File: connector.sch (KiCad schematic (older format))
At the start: 3 parts, among them J1 DB26_Male_HighDensity_Mountin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, J6 Conn_02x02_Odd_Even

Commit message: create footprints
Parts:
- J6: footprint (none) -> Connector_PinHeader_2.54mm:PinHeader_2x02_P2.54mm_Vertical
- SW3: renamed from SW?; footprint (none) -> Button_Switch_THT:SW_DIP_SPSTx03_Slide_9.78x9.8mm_W7.62mm_P2.54mm
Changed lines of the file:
@@
 $Descr A4 11693 8268
 encoding utf-8
-Sheet 7 17
+Sheet 17 17
 Title ""
 Date ""
@@
 AR Path="/5F112860/5F10EEE2/5F14DCB5" Ref="J14"  Part="1"
 AR Path="/5F112863/5F10EEE2/5F14DCB5" Ref="J16"  Part="1"
-F 0 "J6" H 5425 6217 50  0000 C CNN
+F 0 "J16" H 5425 6217 50  0000 C CNN
 F 1 "DB26_Male_HighDensity_MountingHoles" H 5425 6126 50  0000 C CNN
 F 2 "Connector_Dsub:DSUB-26-HD_Male_Horizontal_P2.29x1.98mm_EdgePinOffset3.03mm_Housed_MountingHolesOffset4.94mm" H 4475 5000 50  0001 C CNN
@@
 AR Path="/5F112860/5F10EEE2/5F139BC3" Ref="J15"  Part="1"
 AR Path="/5F112863/5F10EEE2/5F139BC3" Ref="J17"  Part="1"
-F 0 "J7" H 5550 2100 50  0000 C CNN
+F 0 "J17" H 5550 2100 50  0000 C CNN
 F 1 "Conn_02x02_Odd_Even" H 5550 2191 50  0000 C CNN
-F 2 "" H 5500 2425 50  0001 C CNN
+F 2 "Connector_PinHeader_2.54mm:PinHeader_2x02_P2.54mm_Vertical" H 5500 2425 50  0001 C CNN
 F 3 "~" H 5500 2425 50  0001 C CNN
 	1    5500 2425
@@
 AR Path="/5F112860/5F10EEE2/5F4B7169" Ref="#PWR031"  Part="1"
 AR Path="/5F112863/5F10EEE2/5F4B7169" Ref="#PWR034"  Part="1"
-F 0 "#PWR019" H 4525 3150 50  0001 C CNN
+F 0 "#PWR034" H 4525 3150 50  0001 C CNN
 F 1 "GND" H 4530 3227 50  0000 C CNN
 F 2 "" H 4525 3400 50  0001 C CNN
@@
 AR Path="/5F112860/5F10EEE2/5F4B88F0" Ref="#PWR032"  Part="1"
 AR Path="/5F112863/5F10EEE2/5F4B88F0" Ref="#PWR035"  Part="1"
-F 0 "#PWR020" H 5425 5050 50  0001 C CNN
+F 0 "#PWR035" H 5425 5050 50  0001 C CNN
 F 1 "GND" H 5430 5127 50  0000 C CNN
 F 2 "" H 5425 5300 50  0001 C CNN
@@
 5V
 $Comp
-L Switch:SW_DIP_x03 SW?
+L Switch:SW_DIP_x03 SW3
 U 1 1 5F14E492
 P 2975 3575
-AR Path="/5F1123F9/5F10EEE2/5F14E492" Ref="SW?"  Part="1"
-AR Path="/5F11264C/5F10EEE2/5F14E492" Ref="SW?"  Part="1"
-F 0 "SW?" H 2975 4042 50  0000 C CNN
+AR Path="/5F1123F9/5F10EEE2/5F14E492" Ref="SW3"  Part="1"
+AR Path="/5F11264C/5F10EEE2/5F14E492" Ref="SW4"  Part="1"
+AR Path="/5F10DACE/5F10EEE2/5F14E492" Ref="SW2"  Part="1"
+AR Path="/5F11264F/5F10EEE2/5F14E492" Ref="SW5"  Part="1"
+AR Path="/5F11285A/5F10EEE2/5F14E492" Ref="SW6"  Part="1"
+AR Path="/5F11285D/5F10EEE2/5F14E492" Ref="SW7"  Part="1"
+AR Path="/5F112860/5F10EEE2/5F14E492" Ref="SW8"  Part="1"
+AR Path="/5F112863/5F10EEE2/5F14E492" Ref="SW9"  Part="1"
+F 0 "SW9" H 2975 4042 50  0000 C CNN
 F 1 "SW_DIP_x03" H 2975 3951 50  0000 C CNN
-F 2 "" H 2975 3575 50  0001 C CNN
+F 2 "Button_Switch_THT:SW_DIP_SPSTx03_Slide_9.78x9.8mm_W7.62mm_P2.54mm" H 2975 3575 50  0001 C CNN
 F 3 "~" H 2975 3575 50  0001 C CNN
 	1    2975 3575
@@
 AR Path="/5F112860/5F10EEE2/5F4B6D92" Ref="#PWR030"  Part="1"
 AR Path="/5F112863/5F10EEE2/5F4B6D92" Ref="#PWR033"  Part="1"
-F 0 "#PWR018" H 2675 3225 50  0001 C CNN
+F 0 "#PWR033" H 2675 3225 50  0001 C CNN
 F 1 "VCC" V 2675 3575 50  0000 C CNN
 F 2 "" H 2675 3375 50  0001 C CNN

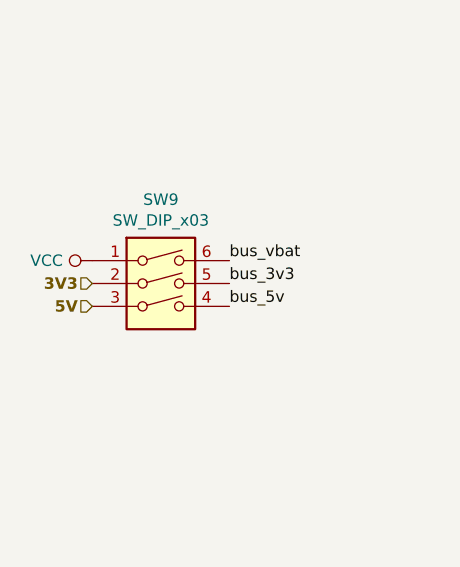
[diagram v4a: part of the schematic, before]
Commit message: rework power management schematic
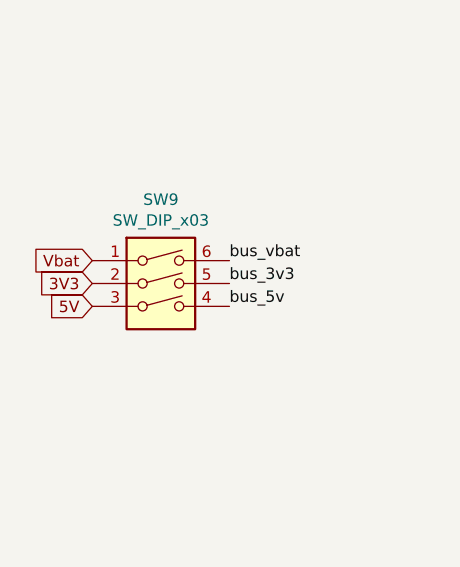
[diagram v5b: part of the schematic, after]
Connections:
- net VCC renamed Vbat
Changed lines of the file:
@@
 $Descr A4 11693 8268
 encoding utf-8
-Sheet 17 17
+Sheet 2 9
 Title ""
 Date ""
@@
 AR Path="/5F112860/5F10EEE2/5F14DCB5" Ref="J14"  Part="1"
 AR Path="/5F112863/5F10EEE2/5F14DCB5" Ref="J16"  Part="1"
+AR Path="/5F1F8EB1/5F14DCB5" Ref="J2"  Part="1"
+AR Path="/5F202513/5F14DCB5" Ref="J?"  Part="1"
+AR Path="/5F214496/5F14DCB5" Ref="J?"  Part="1"
+AR Path="/5F2144C2/5F14DCB5" Ref="J?"  Part="1"
+AR Path="/5F21C578/5F14DCB5" Ref="J?"  Part="1"
+AR Path="/5F21C5A4/5F14DCB5" Ref="J?"  Part="1"
+AR Path="/5F21C5D0/5F14DCB5" Ref="J?"  Part="1"
+AR Path="/5F21C5FC/5F14DCB5" Ref="J?"  Part="1"
+AR Path="/5F22A1CE/5F14DCB5" Ref="J4"  Part="1"
+AR Path="/5F22D207/5F14DCB5" Ref="J6"  Part="1"
+AR Path="/5F22D233/5F14DCB5" Ref="J8"  Part="1"
+AR Path="/5F2317AE/5F14DCB5" Ref="J10"  Part="1"
+AR Path="/5F2317DA/5F14DCB5" Ref="J12"  Part="1"
+AR Path="/5F237BED/5F14DCB5" Ref="J14"  Part="1"
+AR Path="/5F237C19/5F14DCB5" Ref="J16"  Part="1"
 F 0 "J16" H 5425 6217 50  0000 C CNN
 F 1 "DB26_Male_HighDensity_MountingHoles" H 5425 6126 50  0000 C CNN
@@
 AR Path="/5F112860/5F10EEE2/5F139BC3" Ref="J15"  Part="1"
 AR Path="/5F112863/5F10EEE2/5F139BC3" Ref="J17"  Part="1"
+AR Path="/5F1F8EB1/5F139BC3" Ref="J3"  Part="1"
+AR Path="/5F202513/5F139BC3" Ref="J?"  Part="1"
+AR Path="/5F214496/5F139BC3" Ref="J?"  Part="1"
+AR Path="/5F2144C2/5F139BC3" Ref="J?"  Part="1"
+AR Path="/5F21C578/5F139BC3" Ref="J?"  Part="1"
+AR Path="/5F21C5A4/5F139BC3" Ref="J?"  Part="1"
+AR Path="/5F21C5D0/5F139BC3" Ref="J?"  Part="1"
+AR Path="/5F21C5FC/5F139BC3" Ref="J?"  Part="1"
+AR Path="/5F22A1CE/5F139BC3" Ref="J5"  Part="1"
+AR Path="/5F22D207/5F139BC3" Ref="J7"  Part="1"
+AR Path="/5F22D233/5F139BC3" Ref="J9"  Part="1"
+AR Path="/5F2317AE/5F139BC3" Ref="J11"  Part="1"
+AR Path="/5F2317DA/5F139BC3" Ref="J13"  Part="1"
+AR Path="/5F237BED/5F139BC3" Ref="J15"  Part="1"
+AR Path="/5F237C19/5F139BC3" Ref="J17"  Part="1"
 F 0 "J17" H 5550 2100 50  0000 C CNN
 F 1 "Conn_02x02_Odd_Even" H 5550 2191 50  0000 C CNN
@@
 AR Path="/5F112860/5F10EEE2/5F4B7169" Ref="#PWR031"  Part="1"
 AR Path="/5F112863/5F10EEE2/5F4B7169" Ref="#PWR034"  Part="1"
-F 0 "#PWR034" H 4525 3150 50  0001 C CNN
+AR Path="/5F1F8EB1/5F4B7169" Ref="#PWR0102"  Part="1"
+AR Path="/5F202513/5F4B7169" Ref="#PWR?"  Part="1"
+AR Path="/5F214496/5F4B7169" Ref="#PWR?"  Part="1"
+AR Path="/5F2144C2/5F4B7169" Ref="#PWR?"  Part="1"
+AR Path="/5F21C578/5F4B7169" Ref="#PWR?"  Part="1"
+AR Path="/5F21C5A4/5F4B7169" Ref="#PWR?"  Part="1"
+AR Path="/5F21C5D0/5F4B7169" Ref="#PWR?"  Part="1"
+AR Path="/5F21C5FC/5F4B7169" Ref="#PWR?"  Part="1"
+AR Path="/5F22A1CE/5F4B7169" Ref="#PWR0105"  Part="1"
+AR Path="/5F22D207/5F4B7169" Ref="#PWR0108"  Part="1"
+AR Path="/5F22D233/5F4B7169" Ref="#PWR0111"  Part="1"
+AR Path="/5F2317AE/5F4B7169" Ref="#PWR0114"  Part="1"
+AR Path="/5F2317DA/5F4B7169" Ref="#PWR0117"  Part="1"
+AR Path="/5F237BED/5F4B7169" Ref="#PWR0120"  Part="1"
+AR Path="/5F237C19/5F4B7169" Ref="#PWR0123"  Part="1"
+F 0 "#PWR0123" H 4525 3150 50  0001 C CNN
 F 1 "GND" H 4530 3227 50  0000 C CNN
 F 2 "" H 4525 3400 50  0001 C CNN
@@
 AR Path="/5F112860/5F10EEE2/5F4B88F0" Ref="#PWR032"  Part="1"
 AR Path="/5F112863/5F10EEE2/5F4B88F0" Ref="#PWR035"  Part="1"
-F 0 "#PWR035" H 5425 5050 50  0001 C CNN
+AR Path="/5F1F8EB1/5F4B88F0" Ref="#PWR0103"  Part="1"
+AR Path="/5F202513/5F4B88F0" Ref="#PWR?"  Part="1"
+AR Path="/5F214496/5F4B88F0" Ref="#PWR?"  Part="1"
+AR Path="/5F2144C2/5F4B88F0" Ref="#PWR?"  Part="1"
+AR Path="/5F21C578/5F4B88F0" Ref="#PWR?"  Part="1"
+AR Path="/5F21C5A4/5F4B88F0" Ref="#PWR?"  Part="1"
+AR Path="/5F21C5D0/5F4B88F0" Ref="#PWR?"  Part="1"
+AR Path="/5F21C5FC/5F4B88F0" Ref="#PWR?"  Part="1"
+AR Path="/5F22A1CE/5F4B88F0" Ref="#PWR0106"  Part="1"
+AR Path="/5F22D207/5F4B88F0" Ref="#PWR0109"  Part="1"
+AR Path="/5F22D233/5F4B88F0" Ref="#PWR0112"  Part="1"
+AR Path="/5F2317AE/5F4B88F0" Ref="#PWR0115"  Part="1"
+AR Path="/5F2317DA/5F4B88F0" Ref="#PWR0118"  Part="1"
+AR Path="/5F237BED/5F4B88F0" Ref="#PWR0121"  Part="1"
+AR Path="/5F237C19/5F4B88F0" Ref="#PWR0124"  Part="1"
+F 0 "#PWR0124" H 5425 5050 50  0001 C CNN
 F 1 "GND" H 5430 5127 50  0000 C CNN
 F 2 "" H 5425 5300 50  0001 C CNN
@@
 	1    0    0    -1
 $EndComp
-Text HLabel 2675 3475 0    50   Input ~ 10
-3V3
-Text HLabel 2675 3575 0    50   Input ~ 10
-5V
 $Comp
 L Switch:SW_DIP_x03 SW3
@@
 AR Path="/5F112860/5F10EEE2/5F14E492" Ref="SW8"  Part="1"
 AR Path="/5F112863/5F10EEE2/5F14E492" Ref="SW9"  Part="1"
+AR Path="/5F1F8EB1/5F14E492" Ref="SW2"  Part="1"
+AR Path="/5F202513/5F14E492" Ref="SW?"  Part="1"
+AR Path="/5F214496/5F14E492" Ref="SW?"  Part="1"
+AR Path="/5F2144C2/5F14E492" Ref="SW?"  Part="1"
+AR Path="/5F21C578/5F14E492" Ref="SW?"  Part="1"
+AR Path="/5F21C5A4/5F14E492" Ref="SW?"  Part="1"
+AR Path="/5F21C5D0/5F14E492" Ref="SW?"  Part="1"
+AR Path="/5F21C5FC/5F14E492" Ref="SW?"  Part="1"
+AR Path="/5F22A1CE/5F14E492" Ref="SW3"  Part="1"
+AR Path="/5F22D207/5F14E492" Ref="SW4"  Part="1"
+AR Path="/5F22D233/5F14E492" Ref="SW5"  Part="1"
+AR Path="/5F2317AE/5F14E492" Ref="SW6"  Part="1"
+AR Path="/5F2317DA/5F14E492" Ref="SW7"  Part="1"
+AR Path="/5F237BED/5F14E492" Ref="SW8"  Part="1"
+AR Path="/5F237C19/5F14E492" Ref="SW9"  Part="1"
 F 0 "SW9" H 2975 4042 50  0000 C CNN
 F 1 "SW_DIP_x03" H 2975 3951 50  0000 C CNN
@@
 	1    2975 3575
 	1    0    0    -1
-$EndComp
-$Comp
-L power:VCC #PWR012
-U 1 1 5F4B6D92
-P 2675 3375
-AR Path="/5F10DACE/5F10EEE2/5F4B6D92" Ref="#PWR012"  Part="1"
-AR Path="/5F1100AF/5F10EEE2/5F4B6D92" Ref="#PWR?"  Part="1"
-AR Path="/5F1100FD/5F10EEE2/5F4B6D92" Ref="#PWR?"  Part="1"
-AR Path="/5F110145/5F10EEE2/5F4B6D92" Ref="#PWR?"  Part="1"
-AR Path="/5F11031E/5F10EEE2/5F4B6D92" Ref="#PWR?"  Part="1"
-AR Path="/5F110320/5F10EEE2/5F4B6D92" Ref="#PWR?"  Part="1"
-AR Path="/5F110322/5F10EEE2/5F4B6D92" Ref="#PWR?"  Part="1"
-AR Path="/5F110324/5F10EEE2/5F4B6D92" Ref="#PWR?"  Part="1"
-AR Path="/5F1123F9/5F10EEE2/5F4B6D92" Ref="#PWR015"  Part="1"
-AR Path="/5F11264C/5F10EEE2/5F4B6D92" Ref="#PWR018"  Part="1"
-AR Path="/5F11264F/5F10EEE2/5F4B6D92" Ref="#PWR021"  Part="1"
-AR Path="/5F11285A/5F10EEE2/5F4B6D92" Ref="#PWR024"  Part="1"
-AR Path="/5F11285D/5F10EEE2/5F4B6D92" Ref="#PWR027"  Part="1"
-AR Path="/5F112860/5F10EEE2/5F4B6D92" Ref="#PWR030"  Part="1"
-AR Path="/5F112863/5F10EEE2/5F4B6D92" Ref="#PWR033"  Part="1"
-F 0 "#PWR033" H 2675 3225 50  0001 C CNN
-F 1 "VCC" V 2675 3575 50  0000 C CNN
-F 2 "" H 2675 3375 50  0001 C CNN
-F 3 "" H 2675 3375 50  0001 C CNN
-	1    2675 3375
-	0    -1   -1   0
 $EndComp
 Text Label 3275 3375 0    50   ~ 0
@@
 Text Label 5725 3500 0    50   ~ 0
 bus_3v3
+Text GLabel 2675 3375 0    50   Input ~ 0
+Vbat
+Text GLabel 2675 3475 0    50   Input ~ 0
+3V3
+Text GLabel 2675 3575 0    50   Input ~ 0
+5V
 $EndSCHEMATC

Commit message: try improving positionning
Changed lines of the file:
@@
 AR Path="/5F237BED/5F14DCB5" Ref="J14"  Part="1"
 AR Path="/5F237C19/5F14DCB5" Ref="J16"  Part="1"
-F 0 "J16" H 5425 6217 50  0000 C CNN
+F 0 "J2" H 5425 6217 50  0000 C CNN
 F 1 "DB26_Male_HighDensity_MountingHoles" H 5425 6126 50  0000 C CNN
 F 2 "Connector_Dsub:DSUB-26-HD_Male_Horizontal_P2.29x1.98mm_EdgePinOffset3.03mm_Housed_MountingHolesOffset4.94mm" H 4475 5000 50  0001 C CNN
@@
 AR Path="/5F237BED/5F139BC3" Ref="J15"  Part="1"
 AR Path="/5F237C19/5F139BC3" Ref="J17"  Part="1"
-F 0 "J17" H 5550 2100 50  0000 C CNN
+F 0 "J3" H 5550 2100 50  0000 C CNN
 F 1 "Conn_02x02_Odd_Even" H 5550 2191 50  0000 C CNN
 F 2 "Connector_PinHeader_2.54mm:PinHeader_2x02_P2.54mm_Vertical" H 5500 2425 50  0001 C CNN
@@
 AR Path="/5F237BED/5F4B7169" Ref="#PWR0120"  Part="1"
 AR Path="/5F237C19/5F4B7169" Ref="#PWR0123"  Part="1"
-F 0 "#PWR0123" H 4525 3150 50  0001 C CNN
+F 0 "#PWR0102" H 4525 3150 50  0001 C CNN
 F 1 "GND" H 4530 3227 50  0000 C CNN
 F 2 "" H 4525 3400 50  0001 C CNN
@@
 AR Path="/5F237BED/5F4B88F0" Ref="#PWR0121"  Part="1"
 AR Path="/5F237C19/5F4B88F0" Ref="#PWR0124"  Part="1"
-F 0 "#PWR0124" H 5425 5050 50  0001 C CNN
+F 0 "#PWR0103" H 5425 5050 50  0001 C CNN
 F 1 "GND" H 5430 5127 50  0000 C CNN
 F 2 "" H 5425 5300 50  0001 C CNN
@@
 AR Path="/5F237BED/5F14E492" Ref="SW8"  Part="1"
 AR Path="/5F237C19/5F14E492" Ref="SW9"  Part="1"
-F 0 "SW9" H 2975 4042 50  0000 C CNN
+F 0 "SW2" H 2975 4042 50  0000 C CNN
 F 1 "SW_DIP_x03" H 2975 3951 50  0000 C CNN
 F 2 "Button_Switch_THT:SW_DIP_SPSTx03_Slide_9.78x9.8mm_W7.62mm_P2.54mm" H 2975 3575 50  0001 C CNN

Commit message: minor improvements
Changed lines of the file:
@@
 $Descr A4 11693 8268
 encoding utf-8
-Sheet 2 9
+Sheet 3 9
 Title ""
 Date ""
@@
 AR Path="/5F237BED/5F14DCB5" Ref="J14"  Part="1"
 AR Path="/5F237C19/5F14DCB5" Ref="J16"  Part="1"
-F 0 "J2" H 5425 6217 50  0000 C CNN
+F 0 "J4" H 5425 6217 50  0000 C CNN
 F 1 "DB26_Male_HighDensity_MountingHoles" H 5425 6126 50  0000 C CNN
 F 2 "Connector_Dsub:DSUB-26-HD_Male_Horizontal_P2.29x1.98mm_EdgePinOffset3.03mm_Housed_MountingHolesOffset4.94mm" H 4475 5000 50  0001 C CNN
@@
 AR Path="/5F237BED/5F139BC3" Ref="J15"  Part="1"
 AR Path="/5F237C19/5F139BC3" Ref="J17"  Part="1"
-F 0 "J3" H 5550 2100 50  0000 C CNN
+F 0 "J5" H 5550 2100 50  0000 C CNN
 F 1 "Conn_02x02_Odd_Even" H 5550 2191 50  0000 C CNN
 F 2 "Connector_PinHeader_2.54mm:PinHeader_2x02_P2.54mm_Vertical" H 5500 2425 50  0001 C CNN
@@
 AR Path="/5F237BED/5F4B7169" Ref="#PWR0120"  Part="1"
 AR Path="/5F237C19/5F4B7169" Ref="#PWR0123"  Part="1"
-F 0 "#PWR0102" H 4525 3150 50  0001 C CNN
+F 0 "#PWR0123" H 4525 3150 50  0001 C CNN
 F 1 "GND" H 4530 3227 50  0000 C CNN
 F 2 "" H 4525 3400 50  0001 C CNN
@@
 AR Path="/5F237BED/5F4B88F0" Ref="#PWR0121"  Part="1"
 AR Path="/5F237C19/5F4B88F0" Ref="#PWR0124"  Part="1"
-F 0 "#PWR0103" H 5425 5050 50  0001 C CNN
+F 0 "#PWR0124" H 5425 5050 50  0001 C CNN
 F 1 "GND" H 5430 5127 50  0000 C CNN
 F 2 "" H 5425 5300 50  0001 C CNN
@@
 AR Path="/5F237BED/5F14E492" Ref="SW8"  Part="1"
 AR Path="/5F237C19/5F14E492" Ref="SW9"  Part="1"
-F 0 "SW2" H 2975 4042 50  0000 C CNN
+F 0 "SW3" H 2975 4042 50  0000 C CNN
 F 1 "SW_DIP_x03" H 2975 3951 50  0000 C CNN
 F 2 "Button_Switch_THT:SW_DIP_SPSTx03_Slide_9.78x9.8mm_W7.62mm_P2.54mm" H 2975 3575 50  0001 C CNN
